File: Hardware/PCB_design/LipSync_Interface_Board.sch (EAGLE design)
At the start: 31 parts, among them T1 2N3906, U2 SF_MATE_RN42, U3 MPXV7002

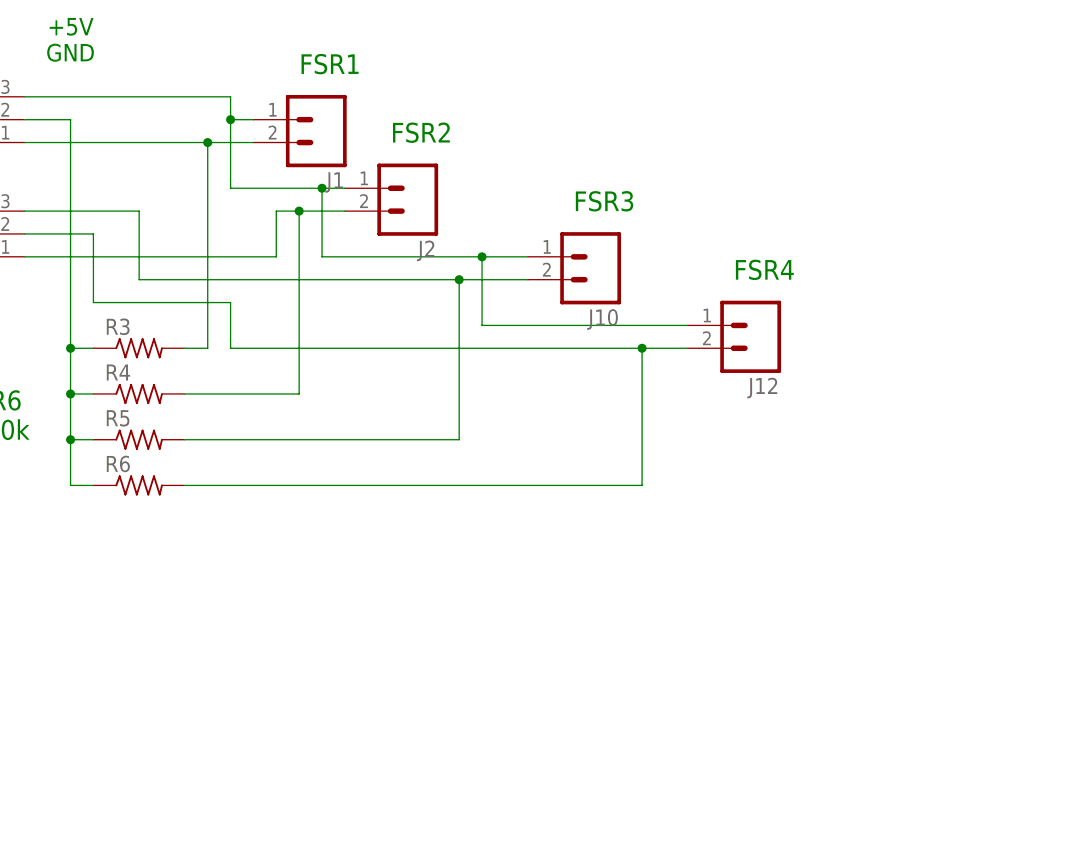
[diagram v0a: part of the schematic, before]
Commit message: Updated PCB eagle files to version 2.7
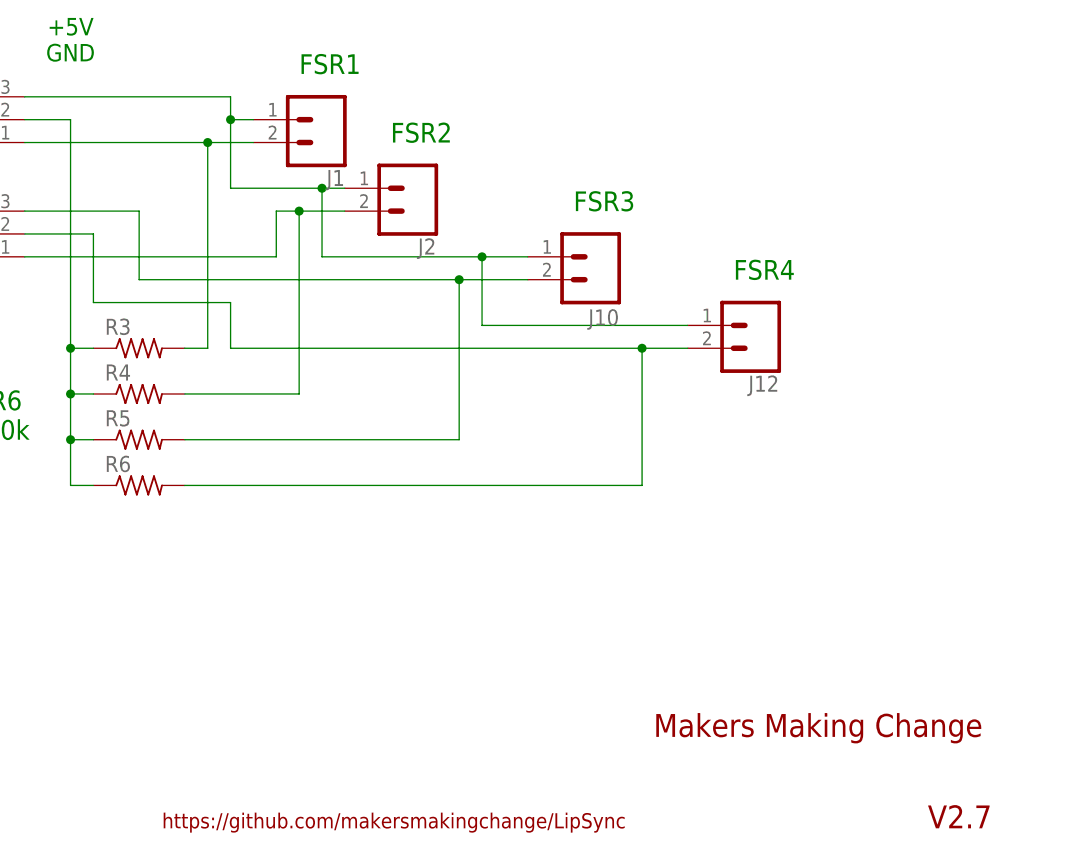
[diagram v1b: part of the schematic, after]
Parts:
- J1, J12, J2: device SparkFun-Connectors:M02PTH -> SparkFun-Connectors:CONN_02PTH3
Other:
- note added: "Makers Making Change"
- note added: "V2.7"
- note added: "https://github.com/makersmakingchange/LipSync"
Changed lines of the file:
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@@
 <?xml version="1.0" encoding="utf-8"?>
 <!DOCTYPE eagle SYSTEM "eagle.dtd">
-<eagle version="7.6.0">
+<eagle version="7.7.0">
 <drawing>
 <settings>
@@
 <layer number="230" name="230bmp" color="7" fill="1" visible="yes" active="yes"/>
 <layer number="231" name="231bmp" color="7" fill="1" visible="yes" active="yes"/>
+<layer number="232" name="Eagle3D_PG2" color="7" fill="1" visible="yes" active="yes"/>
+<layer number="233" name="Eagle3D_PG3" color="7" fill="1" visible="yes" active="yes"/>
 <layer number="248" name="Housing" color="7" fill="1" visible="yes" active="yes"/>
 <layer number="249" name="Edge" color="7" fill="1" visible="yes" active="yes"/>
@@
 <part name="GND6" library="SparkFun-Aesthetics" deviceset="GND" device=""/>
 <part name="GND9" library="SparkFun-Aesthetics" deviceset="GND" device=""/>
-<part name="J1" library="SparkFun-Connectors" deviceset="M02" device="PTH"/>
-<part name="J2" library="SparkFun-Connectors" deviceset="M02" device="PTH"/>
+<part name="J1" library="SparkFun-Connectors" deviceset="CONN_02" device="PTH3"/>
+<part name="J2" library="SparkFun-Connectors" deviceset="CONN_02" device="PTH3"/>
 <part name="J10" library="SparkFun-Connectors" deviceset="M02" device="PTH3"/>
-<part name="J12" library="SparkFun-Connectors" deviceset="M02" device="PTH"/>
+<part name="J12" library="SparkFun-Connectors" deviceset="CONN_02" device="PTH3"/>
 <part name="R3" library="resistor" deviceset="R-US_" device="0204/5"/>
 <part name="R4" library="resistor" deviceset="R-US_" device="0204/5"/>
@@
 <part name="R6" library="resistor" deviceset="R-US_" device="0204/5"/>
 <part name="GND10" library="SparkFun-Aesthetics" deviceset="GND" device=""/>
+<part name="FRAME1" library="frames" deviceset="A3L-LOC" device=""/>
 </parts>
 <sheets>
@@
 <text x="287.02" y="12.7" size="2.1844" layer="91">FSR3</text>
 <text x="304.8" y="5.08" size="2.1844" layer="91">FSR4</text>
+<text x="295.91" y="-45.72" size="2.54" layer="94">Makers Making Change</text>
+<text x="326.39" y="-55.88" size="2.54" layer="94">V2.7</text>
+<text x="241.3" y="-55.88" size="1.6764" layer="94">https://github.com/makersmakingchange/LipSync</text>
 </plain>
 <instances>
@@
 <instance part="R6" gate="G$1" x="238.76" y="-17.78"/>
 <instance part="GND10" gate="1" x="58.42" y="15.24"/>
+<instance part="FRAME1" gate="G$1" x="-48.26" y="-60.96" smashed="yes">
+<attribute name="DRAWING_NAME" x="295.91" y="-40.64" size="2.54" layer="94"/>
+<attribute name="LAST_DATE_TIME" x="295.91" y="-50.8" size="2.286" layer="94"/>
+<attribute name="SHEET" x="309.245" y="-55.88" size="2.54" layer="94"/>
+</instance>
 </instances>
 <busses>

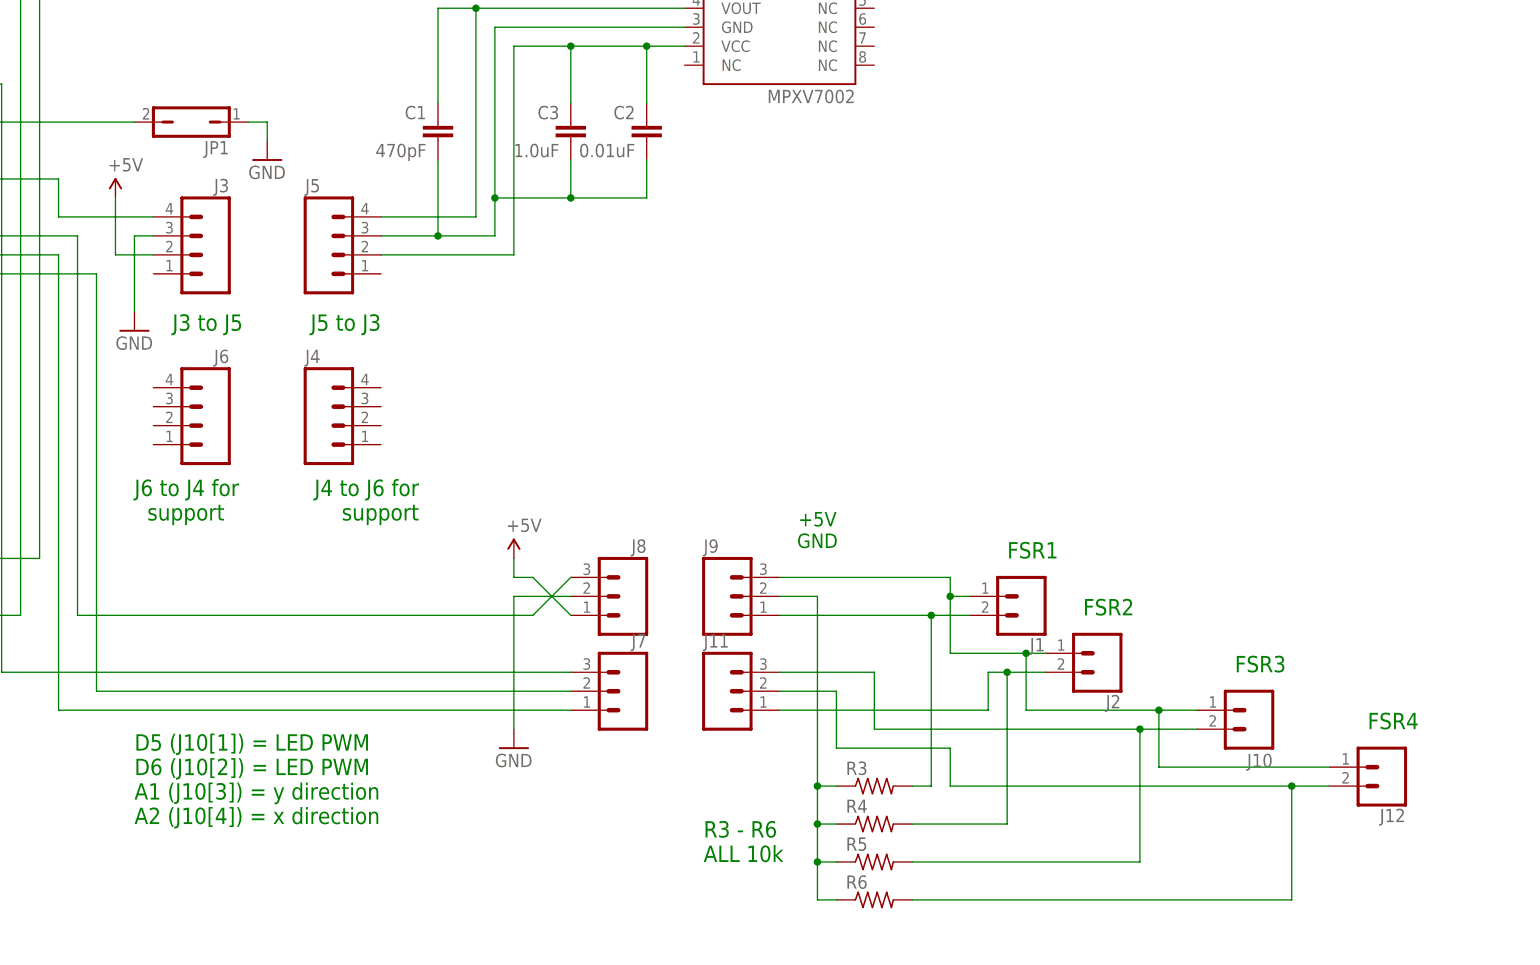
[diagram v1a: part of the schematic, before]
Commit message: Updated Joystick PCB ( Reconnected a trace )
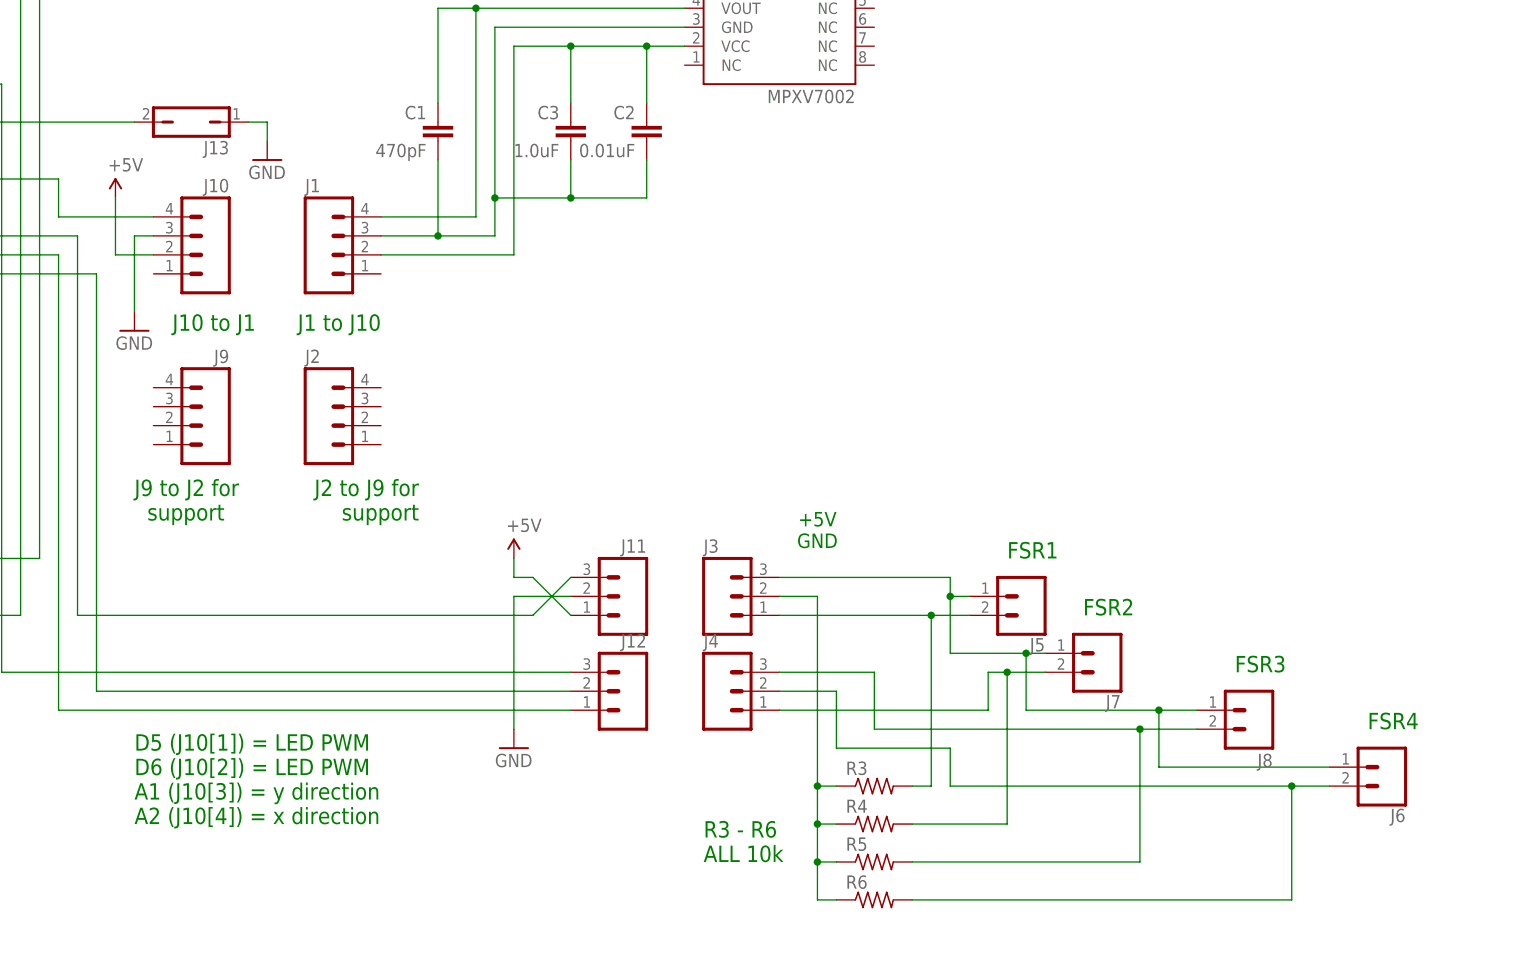
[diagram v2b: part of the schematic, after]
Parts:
- J1, J2: device SparkFun-Connectors:CONN_02PTH3 -> SparkFun-Connectors:M04PTH
- J10: device SparkFun-Connectors:M02PTH3 -> SparkFun-Connectors:M04PTH
- J12: device SparkFun-Connectors:CONN_02PTH3 -> SparkFun-Connectors:M03LOCK
- J3, J4: device SparkFun-Connectors:M04PTH -> SparkFun-Connectors:M03LOCK
- J5, J6: device SparkFun-Connectors:M04PTH -> SparkFun-Connectors:CONN_02PTH3
- J7: device SparkFun-Connectors:M03LOCK -> SparkFun-Connectors:CONN_02PTH3
- J8: device SparkFun-Connectors:M03LOCK -> SparkFun-Connectors:M02PTH3
- J9: device SparkFun-Connectors:M03LOCK -> SparkFun-Connectors:M04PTH
- renumbered JP1 to J13
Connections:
- net GND: now also J10.3, J11.2; no longer J3.3, J8.2
- net GND2: now also J1.3; no longer J5.3
- net GND3: now also J3.2; no longer J9.2
- net N$10: now also J12.3; no longer J7.3
- net N$11: now also J10.4; no longer J3.4
- net N$16: now also J3.3, J5.1, J6.1, J7.1, J8.1; no longer J1.1, J10.1, J12.1, J2.1, J9.3
- net N$21: now also J11.3; no longer J8.3
- net N$22: now also J3.1, J5.2; no longer J1.2, J9.1
- net N$24: now also J4.1, J7.2; no longer J11.1, J2.2
- net N$27: now also J4.3, J8.2; no longer J10.2, J11.3
- net N$28: now also J4.2, J6.2; no longer J11.2, J12.2
- net N$5: now also J12.2; no longer J7.2
- net N$6: now also J12.1; no longer J7.1
- net N$7: now also J1.4; no longer J5.4
- net N$8: now also J1.2; no longer J5.2
- net VCC: now also J10.2, J11.1; no longer J3.2, J8.1
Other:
- note added: "J1 to J10"
- note added: "J10 to J1"
- note added: "J2 to J9 for support"
- note added: "J9 to J2 for support"
- note removed: "J3 to J5"
- note removed: "J4 to J6 for support"
- note removed: "J5 to J3"
- note removed: "J6 to J4 for support"
- moved on the sheet: J11

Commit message: Added PCB files Version 2.71 with updated MMC Logo.
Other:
- note added: "V2.71"
- note removed: "V2.7"
